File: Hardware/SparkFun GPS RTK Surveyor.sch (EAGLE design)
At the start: 94 parts, among them J17 MICRO-SD, J3 USB-C, J4 Qwiic Right Angle, J6 Start Base, J7 Power Switch, Q2 MBT3904DW1T1, U1 MCP73831, U2 3.3V, U3 U-BLOX_ZED-F9P, U5 ESP-WROOM-32NARROW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

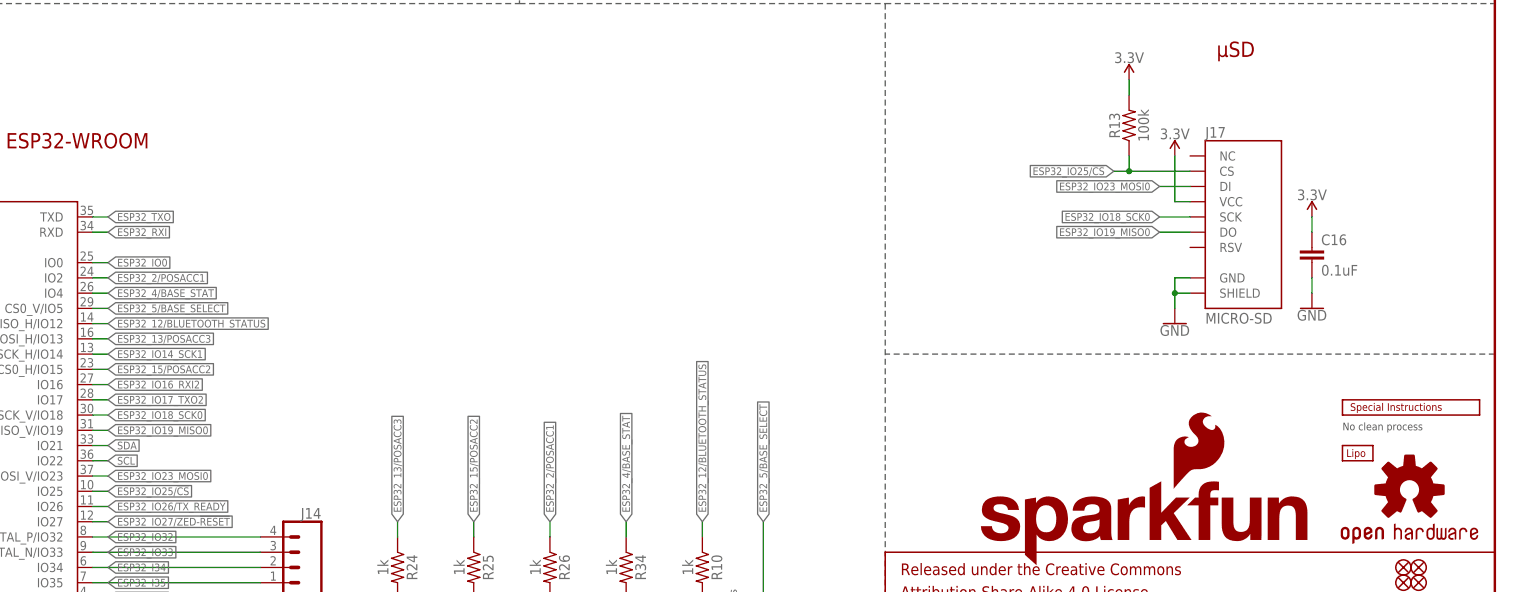
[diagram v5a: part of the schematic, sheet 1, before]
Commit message: Update microSD socket
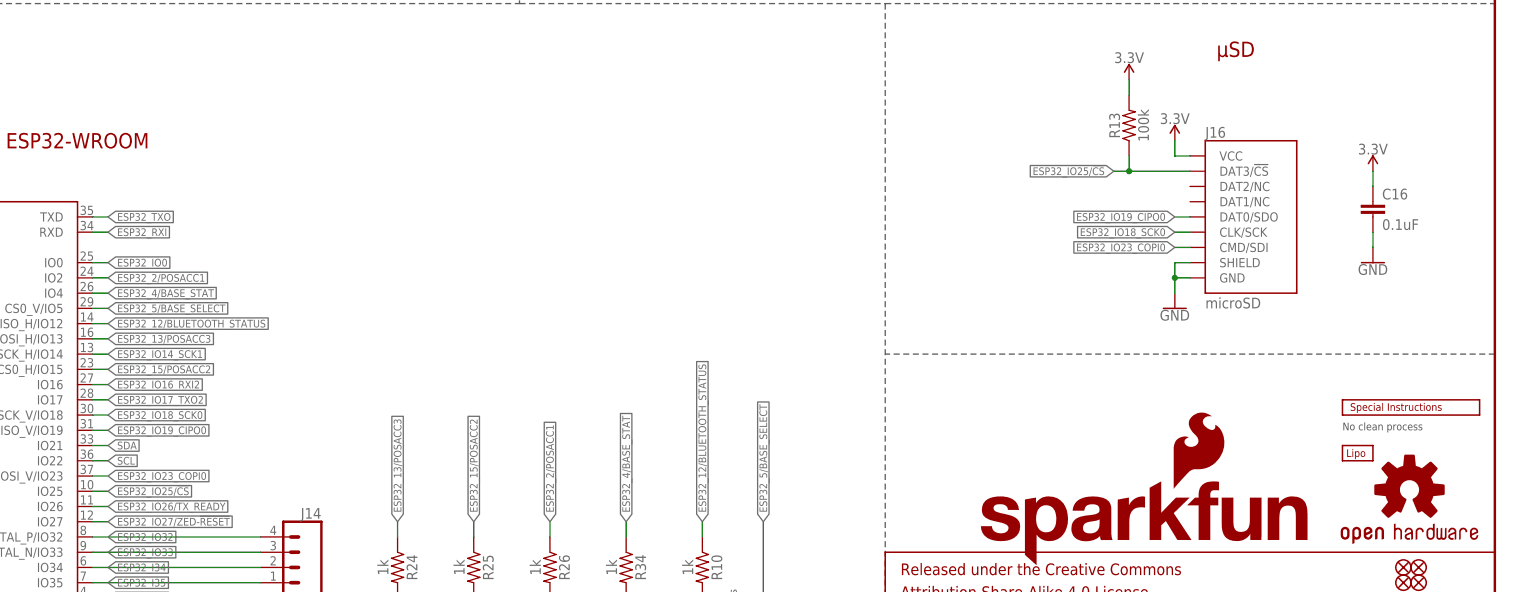
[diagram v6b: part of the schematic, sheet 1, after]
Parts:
- removed J17: MICRO-SD, SparkFun-Connectors:MICRO-SD_CARD_SOCKETPUSH-PUSH
- added J16: microSD, SparkFun-Connectors:MICRO-SD-SDIOPUSH-PUSH
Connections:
- removed net ESP32_IO19_MISO0: J17.DO, U5.MISO_V/IO19
- removed net ESP32_IO23_MOSI0: J17.DI, U5.MOSI_V/IO23
- new net ESP32_IO19_CIPO0: J16.DAT0/SDO, U5.MISO_V/IO19
- new net ESP32_IO23_COPI0: J16.CMD/SDI, U5.MOSI_V/IO23
- net 3.3V: now also J16.VCC; no longer J17.VCC
- net ESP32_IO18_SCK0: now also J16.CLK/SCK; no longer J17.SCK
- net ESP32_IO25/!CS!: now also J16.DAT3/!CS!; no longer J17.CS
- net GND: now also J16.GND, J16.SHIELD; no longer J17.GND, J17.SHIELD
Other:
- moved on the sheet: C16
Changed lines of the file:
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@@
 <part name="SUPPLY19" library="SparkFun-PowerSymbols" deviceset="VIN" device=""/>
 <part name="GND45" library="SparkFun-PowerSymbols" deviceset="GND" device=""/>
-<part name="J17" library="SparkFun-Connectors" deviceset="MICRO-SD_CARD_SOCKET" device="PUSH-PUSH" value="MICRO-SD"/>
 <part name="C16" library="SparkFun-Capacitors" deviceset="0.1UF" device="-0603-25V-(+80/-20%)" value="0.1uF"/>
 <part name="GND46" library="SparkFun-PowerSymbols" deviceset="GND" device=""/>
@@
 <part name="SUPPLY20" library="SparkFun-PowerSymbols" deviceset="VIN" device=""/>
 <part name="SUPPLY7" library="SparkFun-PowerSymbols" deviceset="VIN" device=""/>
+<part name="J16" library="SparkFun-Connectors" deviceset="MICRO-SD-SDIO" device="PUSH-PUSH" value="microSD"/>
 </parts>
 <sheets>
@@
 <attribute name="VALUE" x="198.12" y="165.354" size="1.778" layer="96" align="bottom-center"/>
 </instance>
-<instance part="GND45" gate="1" x="378.46" y="73.66" smashed="yes">
-<attribute name="VALUE" x="378.46" y="73.406" size="1.778" layer="96" align="top-center"/>
-</instance>
-<instance part="J17" gate="J1" x="388.62" y="88.9" smashed="yes">
-<attribute name="NAME" x="383.54" y="104.648" size="1.778" layer="95"/>
-<attribute name="VALUE" x="383.54" y="73.66" size="1.778" layer="96"/>
-</instance>
-<instance part="C16" gate="G$1" x="401.32" y="83.82" smashed="yes">
-<attribute name="NAME" x="402.844" y="86.741" size="1.778" layer="95" font="vector"/>
-<attribute name="VALUE" x="402.844" y="81.661" size="1.778" layer="96" font="vector"/>
-</instance>
-<instance part="GND46" gate="1" x="401.32" y="76.2" smashed="yes">
-<attribute name="VALUE" x="401.32" y="75.946" size="1.778" layer="96" align="top-center"/>
-</instance>
-<instance part="SUPPLY26" gate="G$1" x="378.46" y="101.6" smashed="yes">
-<attribute name="VALUE" x="378.46" y="104.394" size="1.778" layer="96" align="bottom-center"/>
-</instance>
-<instance part="SUPPLY27" gate="G$1" x="401.32" y="91.44" smashed="yes">
-<attribute name="VALUE" x="401.32" y="94.234" size="1.778" layer="96" align="bottom-center"/>
+<instance part="GND45" gate="1" x="378.46" y="76.2" smashed="yes">
+<attribute name="VALUE" x="378.46" y="75.946" size="1.778" layer="96" align="top-center"/>
+</instance>
+<instance part="C16" gate="G$1" x="411.48" y="91.44" smashed="yes">
+<attribute name="NAME" x="413.004" y="94.361" size="1.778" layer="95" font="vector"/>
+<attribute name="VALUE" x="413.004" y="89.281" size="1.778" layer="96" font="vector"/>
+</instance>
+<instance part="GND46" gate="1" x="411.48" y="83.82" smashed="yes">
+<attribute name="VALUE" x="411.48" y="83.566" size="1.778" layer="96" align="top-center"/>
+</instance>
+<instance part="SUPPLY26" gate="G$1" x="378.46" y="104.14" smashed="yes">
+<attribute name="VALUE" x="378.46" y="106.934" size="1.778" layer="96" align="bottom-center"/>
+</instance>
+<instance part="SUPPLY27" gate="G$1" x="411.48" y="99.06" smashed="yes">
+<attribute name="VALUE" x="411.48" y="101.854" size="1.778" layer="96" align="bottom-center"/>
 </instance>
 <instance part="R13" gate="G$1" x="370.84" y="106.68" smashed="yes" rot="R90">
@@
 <instance part="SUPPLY7" gate="G$1" x="302.26" y="243.84" smashed="yes">
 <attribute name="VALUE" x="302.26" y="246.634" size="1.778" layer="96" align="bottom-center"/>
+</instance>
+<instance part="J16" gate="G$1" x="388.62" y="91.44" smashed="yes">
+<attribute name="NAME" x="383.54" y="104.648" size="1.778" layer="95"/>
+<attribute name="VALUE" x="383.54" y="76.2" size="1.778" layer="96"/>
 </instance>
 </instances>
@@
 </segment>
 <segment>
-<wire x1="381" y1="93.98" x2="378.46" y2="93.98" width="0.1524" layer="91"/>
-<wire x1="378.46" y1="93.98" x2="378.46" y2="101.6" width="0.1524" layer="91"/>
-<pinref part="J17" gate="J1" pin="VCC"/>
+<wire x1="381" y1="101.6" x2="378.46" y2="101.6" width="0.1524" layer="91"/>
+<wire x1="378.46" y1="101.6" x2="378.46" y2="104.14" width="0.1524" layer="91"/>
 <pinref part="SUPPLY26" gate="G$1" pin="3.3V"/>
+<pinref part="J16" gate="G$1" pin="VCC"/>
 </segment>
 <segment>
 <pinref part="C16" gate="G$1" pin="1"/>
-<wire x1="401.32" y1="91.44" x2="401.32" y2="88.9" width="0.1524" layer="91"/>
+<wire x1="411.48" y1="99.06" x2="411.48" y2="96.52" width="0.1524" layer="91"/>
 <pinref part="SUPPLY27" gate="G$1" pin="3.3V"/>
 </segment>
@@
 <segment>
 <pinref part="GND45" gate="1" pin="GND"/>
+<wire x1="381" y1="83.82" x2="378.46" y2="83.82" width="0.1524" layer="91"/>
+<wire x1="378.46" y1="83.82" x2="378.46" y2="81.28" width="0.1524" layer="91"/>
+<wire x1="378.46" y1="81.28" x2="378.46" y2="78.74" width="0.1524" layer="91"/>
 <wire x1="381" y1="81.28" x2="378.46" y2="81.28" width="0.1524" layer="91"/>
-<wire x1="378.46" y1="81.28" x2="378.46" y2="78.74" width="0.1524" layer="91"/>
-<wire x1="378.46" y1="78.74" x2="378.46" y2="76.2" width="0.1524" layer="91"/>
-<wire x1="381" y1="78.74" x2="378.46" y2="78.74" width="0.1524" layer="91"/>
-<junction x="378.46" y="78.74"/>
-<pinref part="J17" gate="J1" pin="GND"/>
-<pinref part="J17" gate="J1" pin="SHIELD"/>
+<junction x="378.46" y="81.28"/>
+<pinref part="J16" gate="G$1" pin="GND"/>
+<pinref part="J16" gate="G$1" pin="SHIELD"/>
 </segment>
 <segment>
 <pinref part="C16" gate="G$1" pin="2"/>
 <pinref part="GND46" gate="1" pin="GND"/>
-<wire x1="401.32" y1="78.74" x2="401.32" y2="81.28" width="0.1524" layer="91"/>
+<wire x1="411.48" y1="86.36" x2="411.48" y2="88.9" width="0.1524" layer="91"/>
 </segment>
 </net>
@@
 </segment>
 <segment>
-<pinref part="J17" gate="J1" pin="CS"/>
 <wire x1="381" y1="99.06" x2="370.84" y2="99.06" width="0.1524" layer="91"/>
 <label x="368.3" y="99.06" size="1.27" layer="95" rot="R180" xref="yes"/>
@@
 <wire x1="370.84" y1="101.6" x2="370.84" y2="99.06" width="0.1524" layer="91"/>
 <junction x="370.84" y="99.06"/>
+<pinref part="J16" gate="G$1" pin="DAT3/!CS!"/>
 </segment>
 </net>
@@
 </segment>
 </net>
-<net name="ESP32_IO19_MISO0" class="0">
+<net name="ESP32_IO19_CIPO0" class="0">
 <segment>
 <wire x1="198.12" y1="55.88" x2="200.66" y2="55.88" width="0.1524" layer="91"/>
@@
 </segment>
 <segment>
-<wire x1="381" y1="88.9" x2="375.92" y2="88.9" width="0.1524" layer="91"/>
-<label x="375.92" y="88.9" size="1.27" layer="95" rot="R180" xref="yes"/>
-<pinref part="J17" gate="J1" pin="DO"/>
+<wire x1="381" y1="91.44" x2="378.46" y2="91.44" width="0.1524" layer="91"/>
+<label x="378.46" y="91.44" size="1.27" layer="95" rot="R180" xref="yes"/>
+<pinref part="J16" gate="G$1" pin="DAT0/SDO"/>
 </segment>
 </net>
@@
 </segment>
 <segment>
-<wire x1="381" y1="91.44" x2="375.92" y2="91.44" width="0.1524" layer="91"/>
-<label x="375.92" y="91.44" size="1.27" layer="95" rot="R180" xref="yes"/>
-<pinref part="J17" gate="J1" pin="SCK"/>
+<wire x1="381" y1="88.9" x2="378.46" y2="88.9" width="0.1524" layer="91"/>
+<label x="378.46" y="88.9" size="1.27" layer="95" rot="R180" xref="yes"/>
+<pinref part="J16" gate="G$1" pin="CLK/SCK"/>
 </segment>
 </net>
@@
 </segment>
 </net>
-<net name="ESP32_IO23_MOSI0" class="0">
+<net name="ESP32_IO23_COPI0" class="0">
 <segment>
 <wire x1="198.12" y1="48.26" x2="200.66" y2="48.26" width="0.1524" layer="91"/>
@@
 </segment>
 <segment>
-<wire x1="381" y1="96.52" x2="375.92" y2="96.52" width="0.1524" layer="91"/>
-<label x="375.92" y="96.52" size="1.27" layer="95" rot="R180" xref="yes"/>
-<pinref part="J17" gate="J1" pin="DI"/>
-</segment>
-</net>
+<wire x1="381" y1="86.36" x2="378.46" y2="86.36" width="0.1524" layer="91"/>
+<label x="378.46" y="86.36" size="1.27" layer="95" rot="R180" xref="yes"/>
+<pinref part="J16" gate="G$1" pin="CMD/SDI"/>
+</segment>
+</net>

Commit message: Adjust LEDs to match overlay design.
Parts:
- R1, R10, R11, R12, R24, R25, R26, R34, R8: value 1k -> 330; device SparkFun-Resistors:1KOHM-0603-1/10W-1% -> SparkFun-Resistors:330OHM-0603-1/10W-1%
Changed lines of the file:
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@@
 <?xml version="1.0" encoding="utf-8"?>
 <!DOCTYPE eagle SYSTEM "eagle.dtd">
-<eagle version="9.5.2">
+<eagle version="9.6.2">
 <drawing>
 <settings>
@@
 <part name="SUPPLY5" library="SparkFun-PowerSymbols" deviceset="3.3V" device=""/>
 <part name="R5" library="SparkFun-Resistors" deviceset="3.3KOHM" device="-0603-1/10W-1%" value="3.3k"/>
-<part name="R11" library="SparkFun-Resistors" deviceset="1KOHM" device="-0603-1/10W-1%" value="1k"/>
+<part name="R11" library="SparkFun-Resistors" deviceset="330OHM" device="-0603-1/10W-1%" value="330"/>
 <part name="JP71" library="SparkFun-Aesthetics" deviceset="FIDUCIAL" device="UFIDUCIAL" value="FIDUCIALUFIDUCIAL"/>
 <part name="JP81" library="SparkFun-Aesthetics" deviceset="FIDUCIAL" device="UFIDUCIAL" value="FIDUCIALUFIDUCIAL"/>
@@
 <part name="GND27" library="SparkFun-PowerSymbols" deviceset="GND" device=""/>
 <part name="C4" library="SparkFun-Capacitors" deviceset="1.0UF" device="-0603-16V-10%-X7R" value="1.0uF"/>
-<part name="R1" library="SparkFun-Resistors" deviceset="1KOHM" device="-0603-1/10W-1%" value="1k"/>
+<part name="R1" library="SparkFun-Resistors" deviceset="330OHM" device="-0603-1/10W-1%" value="330"/>
 <part name="LED2" library="SparkFun-LED" deviceset="LED-RED" device="0603" value="RED"/>
 <part name="C5" library="SparkFun-Capacitors" deviceset="0.1UF" device="-0603-25V-5%" value="0.1uF"/>
@@
 <part name="R28" library="SparkFun-Resistors" deviceset="27OHM" device="-0603-1/10W-1%" value="27"/>
 <part name="D3" library="SparkFun-LED" deviceset="LED-WHITE" device="0603" value="WHITE"/>
-<part name="R12" library="SparkFun-Resistors" deviceset="1KOHM" device="-0603-1/10W-1%" value="1k"/>
+<part name="R12" library="SparkFun-Resistors" deviceset="330OHM" device="-0603-1/10W-1%" value="330"/>
 <part name="C1" library="SparkFun-Capacitors" deviceset="47PF" device="-0402-25V-5%-X7R" value="47pF"/>
 <part name="R14" library="SparkFun-Resistors" deviceset="10OHM" device="-0603-1/10W-1%" value="10"/>
@@
 <part name="SUPPLY4" library="SparkFun-PowerSymbols" deviceset="3.3V" device=""/>
 <part name="GND7" library="SparkFun-PowerSymbols" deviceset="GND" device=""/>
-<part name="R34" library="SparkFun-Resistors" deviceset="1KOHM" device="-0603-1/10W-1%" value="1k"/>
+<part name="R34" library="SparkFun-Resistors" deviceset="330OHM" device="-0603-1/10W-1%" value="330"/>
 <part name="D12" library="SparkFun-LED" deviceset="LED-RED" device="0603" value="RED"/>
 <part name="GND58" library="SparkFun-PowerSymbols" deviceset="GND" device=""/>
@@
 <part name="C9" library="SparkFun-Capacitors" deviceset="4.7UF" device="-0603-35V-(20%)" value="4.7uF"/>
 <part name="D5" library="SparkFun-LED" deviceset="LED-YELLOW" device="0603" value="Yellow"/>
-<part name="R8" library="SparkFun-Resistors" deviceset="1KOHM" device="-0603-1/10W-1%" value="1k"/>
+<part name="R8" library="SparkFun-Resistors" deviceset="330OHM" device="-0603-1/10W-1%" value="330"/>
 <part name="SUPPLY14" library="SparkFun-PowerSymbols" deviceset="V_BATT" device=""/>
 <part name="J8" library="SparkFun-Connectors" deviceset="JST_2MM_MALE" device=""/>
@@
 <part name="GND12" library="SparkFun-PowerSymbols" deviceset="GND" device=""/>
 <part name="D7" library="SparkFun-DiscreteSemi" deviceset="DIODE-SCHOTTKY" device="-BAT60A" value="3A/10V/280mV"/>
-<part name="R24" library="SparkFun-Resistors" deviceset="1KOHM" device="-0603-1/10W-1%" value="1k"/>
+<part name="R24" library="SparkFun-Resistors" deviceset="330OHM" device="-0603-1/10W-1%" value="330"/>
 <part name="D8" library="SparkFun-LED" deviceset="LED-GREEN" device="0603" value="GREEN"/>
 <part name="GND20" library="SparkFun-PowerSymbols" deviceset="GND" device=""/>
-<part name="R25" library="SparkFun-Resistors" deviceset="1KOHM" device="-0603-1/10W-1%" value="1k"/>
+<part name="R25" library="SparkFun-Resistors" deviceset="330OHM" device="-0603-1/10W-1%" value="330"/>
 <part name="D10" library="SparkFun-LED" deviceset="LED-GREEN" device="0603" value="GREEN"/>
 <part name="GND21" library="SparkFun-PowerSymbols" deviceset="GND" device=""/>
-<part name="R26" library="SparkFun-Resistors" deviceset="1KOHM" device="-0603-1/10W-1%" value="1k"/>
+<part name="R26" library="SparkFun-Resistors" deviceset="330OHM" device="-0603-1/10W-1%" value="330"/>
 <part name="D11" library="SparkFun-LED" deviceset="LED-GREEN" device="0603" value="GREEN"/>
 <part name="GND22" library="SparkFun-PowerSymbols" deviceset="GND" device=""/>
@@
 <part name="J2" library="SparkFun-Connectors" deviceset="CONN_04" device="JST-SMD-LOCKING"/>
 <part name="P+2" library="SparkFun-PowerSymbols" deviceset="3.3V" device=""/>
-<part name="R10" library="SparkFun-Resistors" deviceset="1KOHM" device="-0603-1/10W-1%" value="1k"/>
+<part name="R10" library="SparkFun-Resistors" deviceset="330OHM" device="-0603-1/10W-1%" value="330"/>
 <part name="D4" library="SparkFun-LED" deviceset="LED-BLUE" device="0603" value="BLUE"/>
 <part name="GND9" library="SparkFun-PowerSymbols" deviceset="GND" device=""/>

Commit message: v12. Add fuel guage. Move ESP32 connectors to panel edge.
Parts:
- removed D5: Yellow, SparkFun-LED:LED-YELLOW0603
- removed LED2: RED, SparkFun-LED:LED-RED0603
- removed R1, R8: 330, SparkFun-Resistors:330OHM-0603-1/10W-1%
- removed S4: Boot, SparkFun-Switches:MOMENTARY-SWITCH-SPST-SMD-5.2-TALL-REDUNDANT
- added C15: 0.1uF, SparkFun-Capacitors:0.1UF-0603-25V-(+80/-20%)
- added D13: RGB, SparkFun-LED:LED-RGB-CAPLCC
- added MEAS, MEAS1: JUMPER-COMBO_2_NC_TRACE, SparkFun-Jumpers:JUMPER-COMBO_2_NC_TRACE
- added U7: MAX17048, SparkFun-IC-Power:MAX17048DFN8
- J14: device SparkFun-Connectors:CONN_041X04_NO_SILK_NO_POP -> SparkFun-Connectors:CONN_021X02_NO_SILK
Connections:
- net !SAFE! renamed ZED_!SAFE!
- net ESP32_12/BLUETOOTH_STATUS renamed ESP_12/LED_BLUETOOTH
- net ESP32_13/POSACC3 renamed ESP_13/LED_100CM
- net ESP32_15/POSACC2 renamed ESP_15/LED_10CM
- net ESP32_2/POSACC1 renamed ESP_2/LED_1CM
- net ESP32_4/BASE_STAT renamed ESP_4/LED_BASE_STAT
- net ESP32_5/BASE_SELECT renamed ESP_5/SWITCH_BASE_SELECT
- net ESP32_I39 renamed ESP_I39
- net ESP32_IO14_SCK1 renamed ESP_14
- net ESP32_IO16_RXI2 renamed ESP_16/BT_RXI
- net ESP32_IO17_TXO2 renamed ESP_17/BT_TXO
- net ESP32_IO18_SCK0 renamed ESP_18/SD_SCK
- net ESP32_IO19_CIPO0 renamed ESP_19/SD_CIPO
- net ESP32_IO23_COPI0 renamed ESP_23/SD_COPI
- net ESP32_IO25/!CS! renamed ESP_25/SD_!CS!
- net ESP32_IO26/TX_READY renamed ESP_26/ZED_TX_READY
- net ESP32_IO27/ZED-!RESET! renamed ESP_27/ZED_!RESET!
- net FENCE_STAT renamed ZED_FENCE_STAT
- net PPS_STAT renamed ZED_PPS_STAT
- net RTK_STAT renamed ZED_RTK_STAT
- removed net ESP32_I34: J14.2, U5.IO34
- removed net ESP32_I35: J14.1, U5.IO35
- removed net ESP32_I36: U5.SENSOR_VP/I36
- removed net ESP32_IO0: Q2Q2.C, S4.2, U5.IO0
- removed net ESP32_IO32: J14.4, U5.XTAL_P/IO32
- removed net ESP32_IO33: J14.3, U5.XTAL_N/IO33
- removed net N$10: LED2.A, R1.1
- removed net N$8: D5.C, R8.2
- removed net SCL: J4.4, R9B.2, U5.IO22
- removed net SDA: J4.3, R9C.2, U5.IO21
- new net ESP_0/BOOT: Q2Q2.C, U5.IO0
- new net ESP_21/SDA: J4.3, R9C.2, U5.IO21, U7.SDA
- new net ESP_22/SCL: J4.4, R9B.2, U5.IO22, U7.SCL
- new net ESP_32: J14.2, U5.XTAL_P/IO32
- new net ESP_33: J14.1, U5.XTAL_N/IO33
- new net ESP_34/PWR_LVL_RED: D13.RED, U5.IO34
- new net ESP_35/PWR_LVL_GRN: D13.GRN, U5.IO35
- new net ESP_36/BATT_ALRT: U5.SENSOR_VP/I36, U7.!ALRT
- new net N$4: J5.VBUS, MEAS.1
- new net N$7: J8.+, MEAS1.1
- net 3.3V: no longer R1.2
- net CHG_LED: now also D13.BLU; no longer R8.1
- net GND: now also C15.2, U7.CTG, U7.GND, U7.QSTRT; no longer LED2.C, S4.1
- net VIN: now also D13.A, MEAS.2; no longer D5.A, J5.VBUS
- net V_BATT: now also C15.1, MEAS1.2, U7.CELL, U7.VDD; no longer J8.+
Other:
- note added: "Add MEAS jumper to batt"
- note added: "Add batt level leds"
- note added: "Add fuel guage"
- note added: "Bluetooth"
- note added: "Default: Bluetooth will broadcast NMEA. Move switch to 'RTCM' to use Bluetooth as radio connection between RTK units for RTCM corrections."
- note added: "Default: ZED-Serial1 NMEA connected to Bluetooth. Move switch to 'Ext Cntr' to connect external 'Data' connector to ZED-Serial1."
- note added: "Fuel Gauge"
- note added: "Move ESP32 USB to panel edge"
- note added: "Move Qwiic connector"
- note added: "Move microSD to panel edge"
- note added: "NMEA"
- note added: "RTCM"
- note added: "v12"
- note removed: "Add ADC connection to battery level"
- note removed: "Add divider for batt level"
- note removed: "Default: Bluetooth will broadcast NMEA. Move S3 to 'RTCM' to use Bluetooth as radio connection between RTK units for RTCM corrections."
- note removed: "Default: ZED-Serial1 NMEA connected to Bluetooth. Move down to connect external NMEA connector outputs to ZED-Serial1. Move"
- note removed: "v11"
- moved on the sheet: B1, BLUETOOTH_BROADCAST, C16, C3, C4, C5, C6, C8, C9, D1, D2, D3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
